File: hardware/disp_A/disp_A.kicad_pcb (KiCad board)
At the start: 2 copper layers, 82 x 52 mm, 115 parts, among them J1 Conn_02x16_Odd_Even_FLIP, J2 Conn_01x01_Pin, J3 Conn_01x01_Pin, Q1 2N7002, Q10 2N7002, Q11 2N7002, Q12 2N7002, Q13 2N7002, Q2 2N7002, Q3 2N7002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

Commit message: updates
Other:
- board text added: "Disp Rev A.1 Cullen Jennings"
- board text removed: "Disp Rev A Cullen Jennings"
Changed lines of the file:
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@@
 		(title "Disp")
 		(date "2024-05-26")
-		(rev "A")
+		(rev "A.1")
 		(company "Cullen Jennings")
 	)
@@
 		)
 	)
-	(gr_text "Disp Rev A\nCullen Jennings"
+	(gr_text "Disp Rev A.1\nCullen Jennings"
 		(at 234.664442 108.693825 0)
 		(layer "F.SilkS")

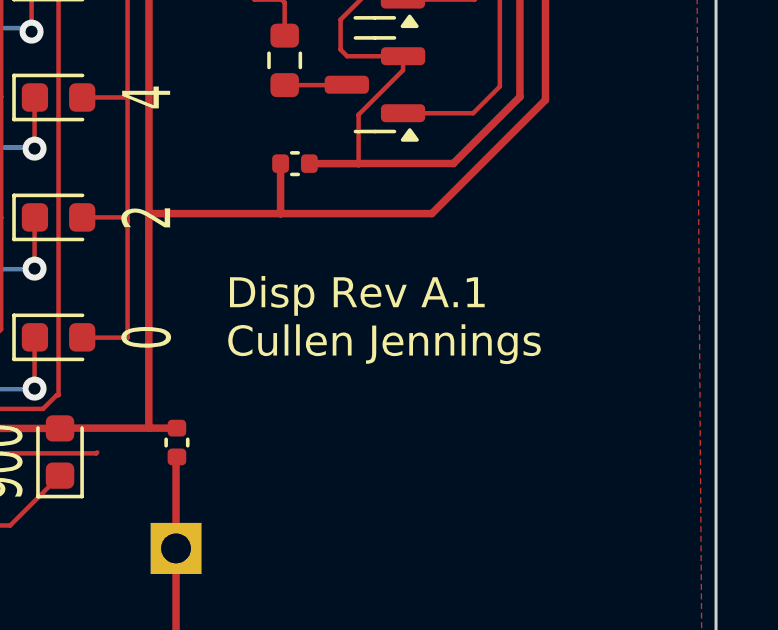
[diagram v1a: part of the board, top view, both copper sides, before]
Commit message: update all harware revs
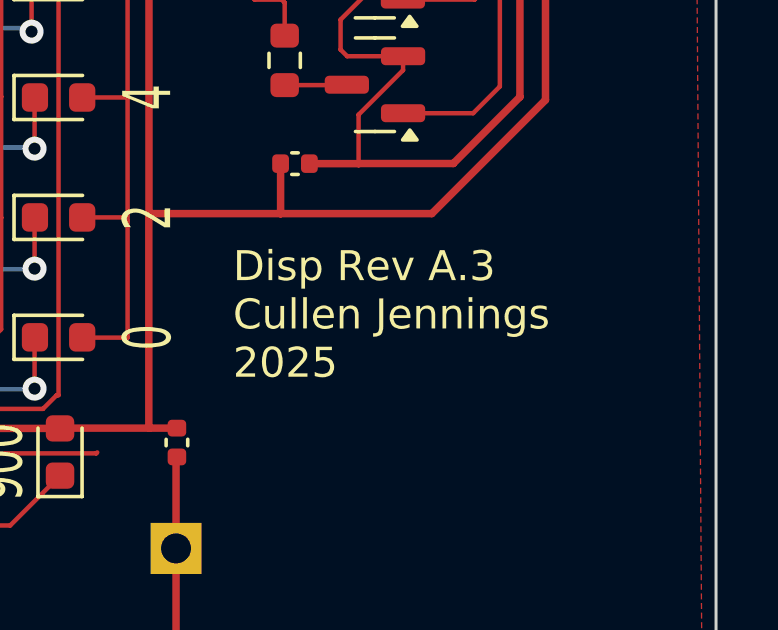
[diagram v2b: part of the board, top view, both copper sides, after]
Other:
- board text added: "Disp Rev A.3 Cullen Jennings 2025"
- board text removed: "Disp Rev A.1 Cullen Jennings"
